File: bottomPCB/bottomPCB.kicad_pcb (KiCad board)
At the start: 2 copper layers, 184.8 x 139 mm, 46 parts, among them J1 Conn_01x03_Pin, J2 Conn_02x03_Odd_Even, J3 Conn_01x02, J4 Conn_02x03_Odd_Even, J5 1-84953-1, J6 1-84953-1, J7 1-84953-1, J8 1-84953-1, U1 ESP32-WROOM-32, U2 XT30_horizontal, U8 LM1117IMPX-3_3_NOPB, U9 LM1117IMPX-3_3_NOPB

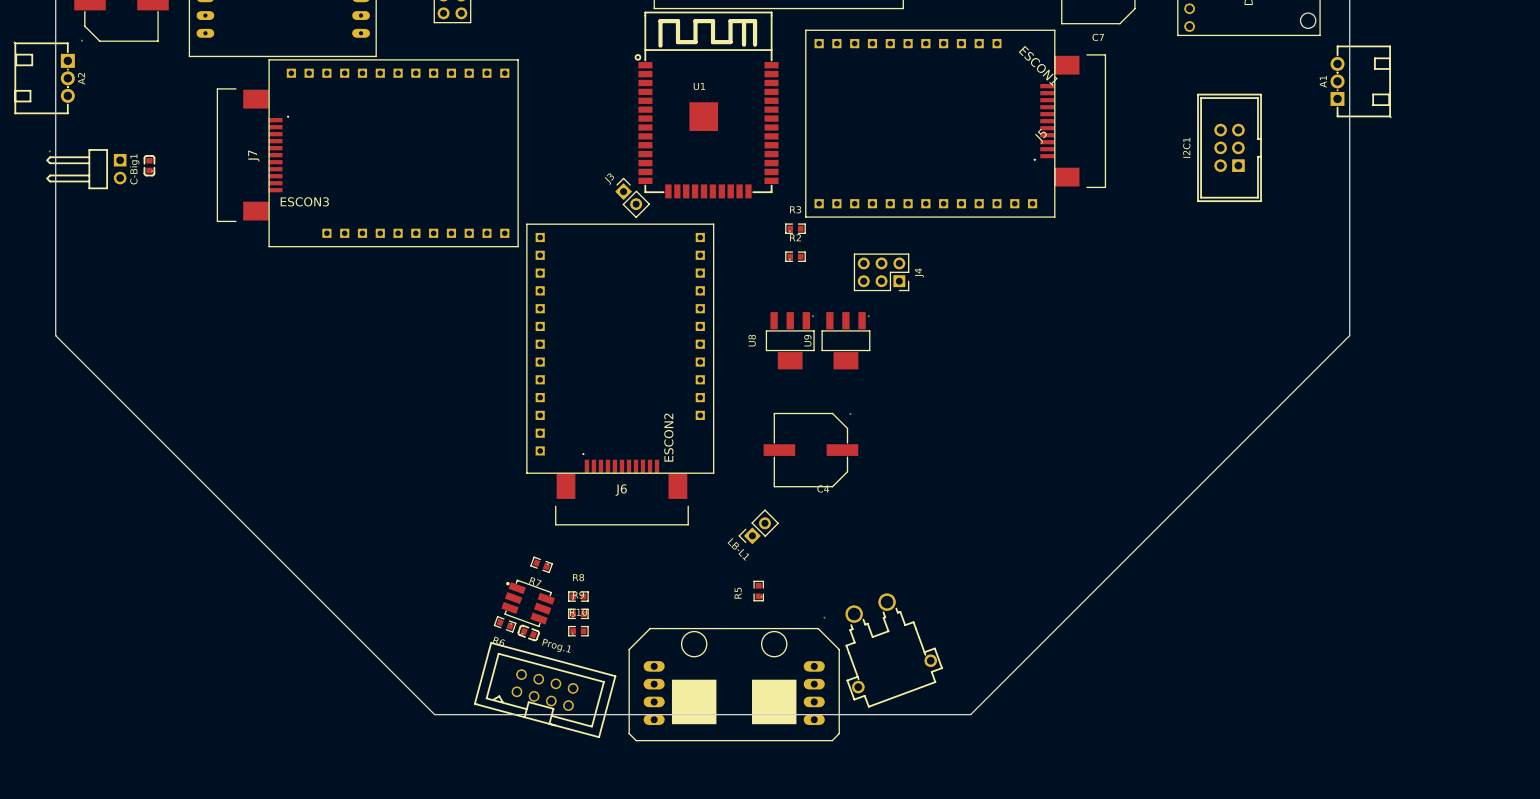
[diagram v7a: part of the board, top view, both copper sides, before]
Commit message: rearranged electronics to fit octagon
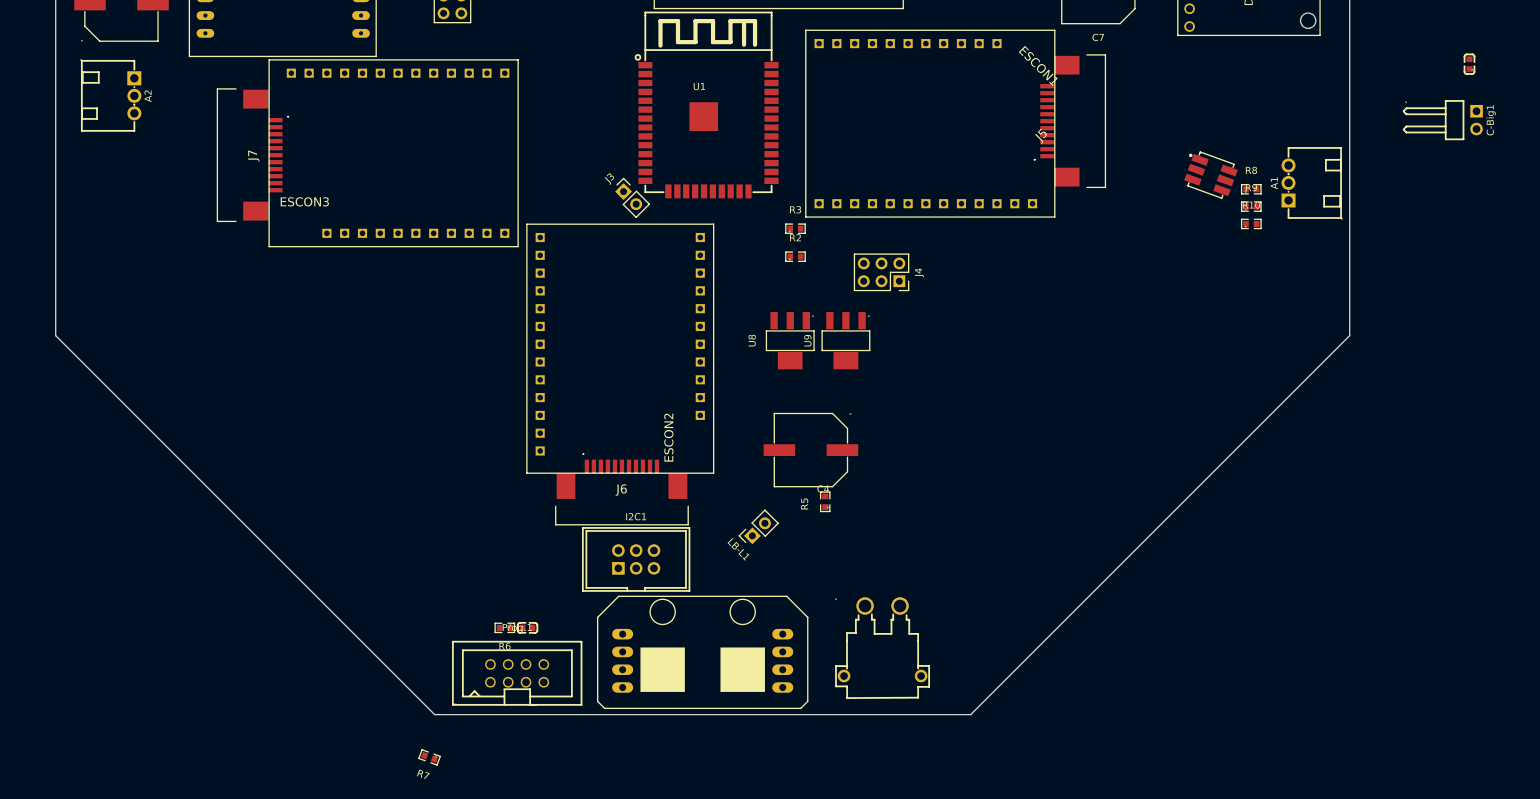
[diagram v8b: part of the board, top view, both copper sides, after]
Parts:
- moved C-Big1 193.8 mm to (120.5, 17.5)
- moved C6 189.1 mm to (119.5, 9.50)
- moved LED1 115.1 mm to (82.6, 25.3)
- moved R8 112.3 mm to (88.3, 27.4)
- moved R10 112.3 mm to (88.3, 32.3)
- moved R9 112.3 mm to (88.3, 29.8)
- moved I2C1 103.1 mm to (0.50, 80.2), turned to 0 degrees
- moved R7 31.8 mm to (-29.0, 108.5)
- moved A1 16.1 mm to (93.7, 26.5)
- moved R5 15.9 mm to (27.5, 72.0)
- moved A2 9.82 mm to (-71.2, 14.0)
- moved Taster_LED1 6.44 mm to (10.0, 91.5)
- moved Prog.1 4.65 mm to (-16.5, 96.5), turned to 0 degrees
- moved C3 0.76 mm to (-15.0, 90.0), turned to 0 degrees
- moved R6 0.50 mm to (-18.3, 90.0), turned to 180 degrees
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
